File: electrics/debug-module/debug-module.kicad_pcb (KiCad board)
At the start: 2 copper layers, 40.6 x 30.4 mm, 25 parts, among them J1 East, J2 West, J3 USB_B_Micro, U1 FT231XS, U2 LD1117S33

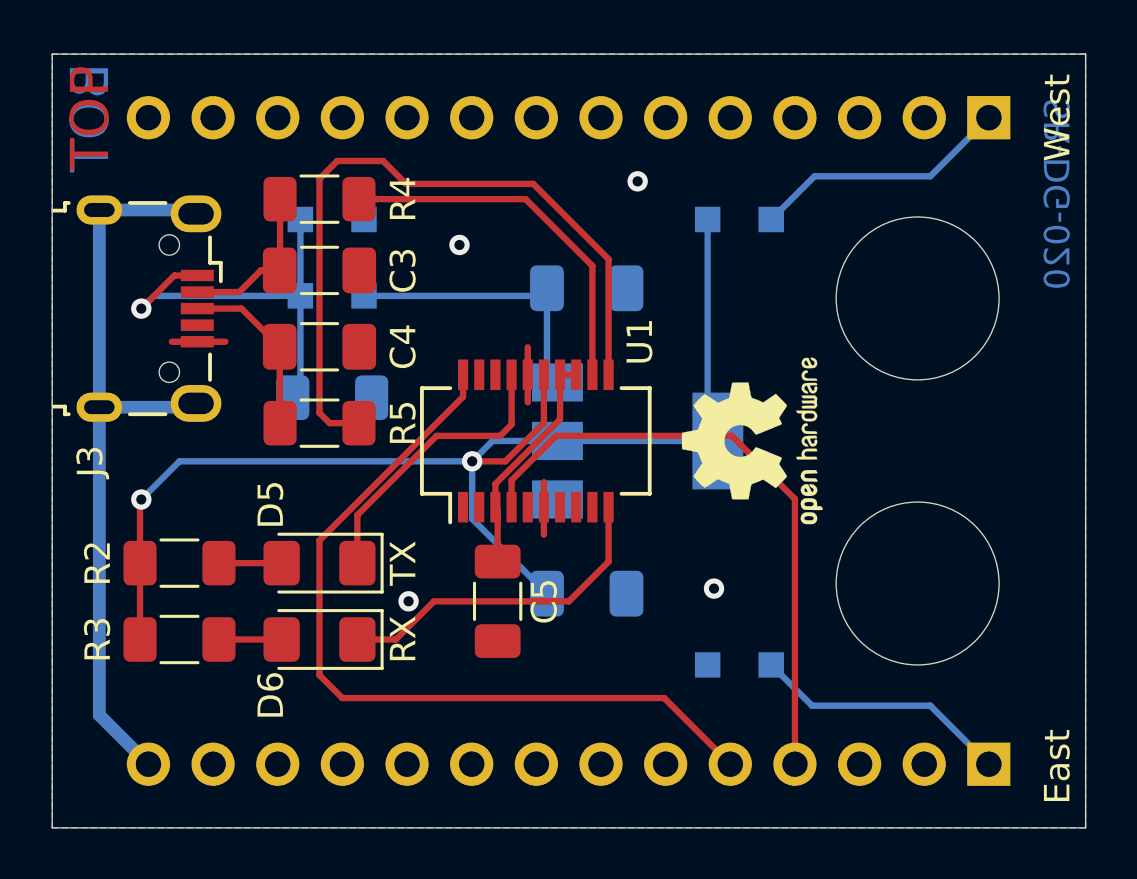
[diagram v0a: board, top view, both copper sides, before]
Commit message: INOA-372 Fix autoprogrammer for debug module
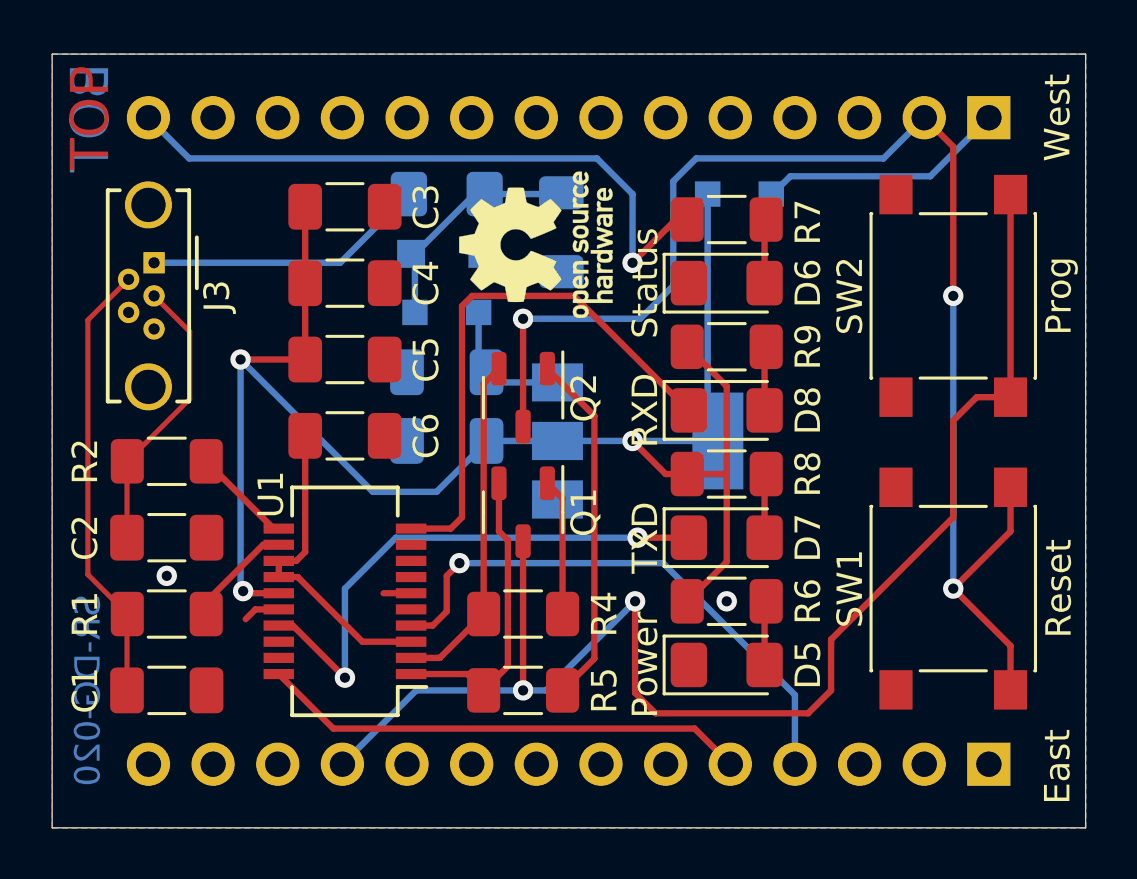
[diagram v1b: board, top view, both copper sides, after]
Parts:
- removed D4: D_Schottky, Diode_SMD:D_SOD-323_HandSoldering
- removed G2: Logo_Open_Hardware_Small, Symbol:OSHW-Logo2_7.3x6mm_SilkScreen
- removed H1: Reset, MountingHole:MountingHole_6.4mm_M6
- removed H2: Status, MountingHole:MountingHole_6.4mm_M6
- added C6: 100nF, Capacitor_SMD:C_1206_3216Metric_Pad1.33x1.80mm_HandSolder, F.Cu at (131.5, 95.0)
- added C7: 100nF, Capacitor_SMD:C_1206_3216Metric_Pad1.33x1.80mm_HandSolder, B.Cu at (135.5, 92.5)
- added C9: 10uF, Capacitor_SMD:C_1206_3216Metric_Pad1.33x1.80mm_HandSolder, B.Cu at (135.5, 95.2)
- added D7: TXD, LED_SMD:LED_1206_3216Metric_Pad1.42x1.75mm_HandSolder, F.Cu at (146.5, 99.0)
- added D8: RXD, LED_SMD:LED_1206_3216Metric_Pad1.42x1.75mm_HandSolder, F.Cu at (146.5, 94.0)
- added F1: 5V/1A, Fuse:Fuse_1206_3216Metric_Pad1.42x1.75mm_HandSolder, B.Cu at (135.5, 85.5)
- added LOGO1: Logo_Open_Hardware_Small, Symbol:OSHW-Logo_5.7x6mm_SilkScreen, F.Cu at (139.0, 87.5)
- added Q1: S8050, Package_TO_SOT_SMD:SOT-23-3, F.Cu at (138.5, 98.0)
- added Q2: S8050, Package_TO_SOT_SMD:SOT-23-3, F.Cu at (138.5, 93.5)
- added R6: 220R, Resistor_SMD:R_1206_3216Metric_Pad1.30x1.75mm_HandSolder, F.Cu at (146.5, 101.5)
- added R7: 220R, Resistor_SMD:R_1206_3216Metric_Pad1.30x1.75mm_HandSolder, F.Cu at (146.5, 86.5)
- added R8: 220R, Resistor_SMD:R_1206_3216Metric_Pad1.30x1.75mm_HandSolder, F.Cu at (146.5, 96.5)
- added R9: 220R, Resistor_SMD:R_1206_3216Metric_Pad1.30x1.75mm_HandSolder, F.Cu at (146.5, 91.5)
- added SW1: Reset, Button_Switch_SMD:SW_SPST_PTS645, F.Cu at (155.4, 101.0)
- added SW2: Prog, Button_Switch_SMD:SW_SPST_PTS645, F.Cu at (155.4, 89.5)
- C1: value 100nF -> 47pF; moved to F.Cu
- C2: value 10uF -> 47pF; moved to F.Cu
- C3: value 47pF -> 4u7
- C4: value 47pF -> 100nF
- D1: value BZT52C6V2 -> MM3Z6V2T1G; footprint Diode_SMD:D_SOD-323_HandSoldering -> Diode_SMD:D_SOD-123F
- D3: value D_Schottky -> 1N5819
- D5: value TX -> Power
- D6: value RX -> Status
- J3: value USB_B_Micro -> USB; footprint Connector_USB:USB_Micro-B_Wuerth_629105150521 -> Connector_USB:USB_Micro-B_Wuerth_614105150721_Vertical_CircularHoles
- R1: value 10k -> 27R; moved to F.Cu
- R2: value 220R -> 27R
- R3: value 220R -> 10k; moved to B.Cu
- R4, R5: value 27R -> 10k
- moved G1 32.6 mm to (124.0, 97.0)
- moved C1 22.8 mm to (124.5, 105.0)
- moved R3 21.9 mm to (140.0, 87.0), turned to 90 degrees
- moved D6 21.3 mm to (146.5, 89.0), turned to 0 degrees
- moved D3 18.5 mm to (147.0, 85.5), turned to 180 degrees
- moved R4 18.2 mm to (138.5, 102.0)
- moved C2 16.6 mm to (124.5, 99.0)
- moved D5 16.5 mm to (146.5, 104.0), turned to 0 degrees
- moved R5 13.2 mm to (138.5, 105.0)
- moved C5 11.2 mm to (131.5, 92.0), turned to 0 degrees
- moved R1 10.7 mm to (124.5, 102.0), turned to 180 degrees
- moved U1 9.79 mm to (131.5, 101.5), turned to 180 degrees
- moved D1 4.70 mm to (135.5, 87.8)
- moved D2 4.55 mm to (135.5, 90.2)
- moved R2 4.03 mm to (124.5, 96.0), turned to 180 degrees
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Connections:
- C1 pad 1: Net-(C1-Pad1) -> D-
- C2 pad 1: +3V3 -> D+
- C3 pad 1: USB_DM -> +3V3
- C4 pad 1: USB_DP -> +3V3
- C5 pad 1: Net-(C5-Pad1) -> +3V3
- D2 pad 1: Net-(C1-Pad1) -> Net-(C7-Pad1)
- D3 pad 1: GND -> Net-(J2-Pad1)
- D3 pad 2: Net-(D3-Pad2) -> +3V3
- D5 pad 1: TX_LED -> GND
- D6 pad 1: RX_LED -> GND
- J1 pad 1: Net-(D3-Pad2) -> GND
- J1 pad 10: (no net) -> unconnected-(J1-Pad10)
- J1 pad 11: (no net) -> IO0
- J1 pad 12: (no net) -> unconnected-(J1-Pad12)
- J1 pad 13: (no net) -> unconnected-(J1-Pad13)
- J1 pad 14: GNDPWR -> GND
- J1 pad 2: (no net) -> unconnected-(J1-Pad2)
- J1 pad 3: (no net) -> unconnected-(J1-Pad3)
- J1 pad 6: (no net) -> unconnected-(J1-Pad6)
- J1 pad 7: (no net) -> unconnected-(J1-Pad7)
- J1 pad 8: (no net) -> unconnected-(J1-Pad8)
- J1 pad 9: (no net) -> unconnected-(J1-Pad9)
- J2 pad 1: Net-(D4-Pad1) -> Net-(J2-Pad1)
- J2 pad 10: (no net) -> unconnected-(J2-Pad10)
- J2 pad 11: (no net) -> unconnected-(J2-Pad11)
- J2 pad 12: (no net) -> unconnected-(J2-Pad12)
- J2 pad 13: (no net) -> unconnected-(J2-Pad13)
- J2 pad 14: (no net) -> IO13
- J2 pad 2: (no net) -> Chip_PU
- J2 pad 3: (no net) -> unconnected-(J2-Pad3)
- J2 pad 4: (no net) -> unconnected-(J2-Pad4)
- J2 pad 5: (no net) -> unconnected-(J2-Pad5)
- J2 pad 6: (no net) -> unconnected-(J2-Pad6)
- J2 pad 7: (no net) -> unconnected-(J2-Pad7)
- J2 pad 8: (no net) -> unconnected-(J2-Pad8)
- J2 pad 9: (no net) -> unconnected-(J2-Pad9)
- J3 pad 1: Net-(D1-Pad1) -> Net-(F1-Pad1)
- J3 pad 2: USB_DM -> D-
- J3 pad 3: USB_DP -> D+
- J3 pad 4: (no net) -> unconnected-(J3-Pad4)
- J3 pad 6: GNDPWR -> GND
- R1 pad 1: Net-(D1-Pad1) -> Net-(R1-Pad1)
- R1 pad 2: GND -> D-
- R2 pad 1: +3V3 -> Net-(R2-Pad1)
- R2 pad 2: Net-(D5-Pad2) -> D+
- R3 pad 1: +3V3 -> GND
- R3 pad 2: Net-(D6-Pad2) -> Net-(D1-Pad1)
- R4 pad 1: Net-(R4-Pad1) -> Net-(Q1-Pad1)
- R4 pad 2: USB_DM -> FT_~{RTS}
- R5 pad 1: Net-(R5-Pad1) -> Net-(Q2-Pad1)
- R5 pad 2: USB_DP -> FT_~{DTR}
- U1 pad 1: (no net) -> FT_~{DTR}
- U1 pad 11: Net-(R5-Pad1) -> Net-(R2-Pad1)
- U1 pad 12: Net-(R4-Pad1) -> Net-(R1-Pad1)
- U1 pad 13: Net-(C5-Pad1) -> Net-(C6-Pad1)
- U1 pad 14: Net-(C5-Pad1) -> Net-(C6-Pad1)
- U1 pad 18: (no net) -> unconnected-(U1-Pad18)
- U1 pad 19: (no net) -> unconnected-(U1-Pad19)
- U1 pad 2: (no net) -> FT_~{RTS}
- U1 pad 3: Net-(C5-Pad1) -> Net-(C6-Pad1)
- U1 pad 5: (no net) -> unconnected-(U1-Pad5)
- U1 pad 7: (no net) -> unconnected-(U1-Pad7)
- U1 pad 8: (no net) -> unconnected-(U1-Pad8)
- U1 pad 9: (no net) -> unconnected-(U1-Pad9)
- U2 pad 3: Net-(C1-Pad1) -> Net-(C7-Pad1)
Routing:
- net IO0: track 0.00 -> 55.2 mm, vias 0 -> 2
- net Chip_PU: track 0.00 -> 54.5 mm, vias 0 -> 3
- net GNDPWR: track 30.3 -> 0.00 mm
- net Net-(R5-Pad1): track 28.7 -> 0.00 mm
- net IO13: track 0.00 -> 25.8 mm, vias 0 -> 1
- net D-: track 0.00 -> 17.5 mm
- net +3V3: track 49.7 -> 66.3 mm, vias 2 -> 3
- net Net-(R4-Pad1): track 14.5 -> 0.00 mm
- net Net-(Q2-Pad1): track 0.00 -> 13.9 mm
- net FT_~{RTS}: track 0.00 -> 13.4 mm
- net Net-(C6-Pad1): track 0.00 -> 12.6 mm
- net U0RXD: track 31.7 -> 19.2 mm
- net FT_~{DTR}: track 0.00 -> 11.8 mm
- net Net-(C1-Pad1): track 11.2 -> 0.00 mm
- net Net-(F1-Pad1): track 0.00 -> 11.1 mm
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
